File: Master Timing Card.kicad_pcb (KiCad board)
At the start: 4 copper layers, 170 x 100 mm, 250 parts, among them CN1 Pin_03, CN10 M2 x 2.5mm, CN11 UE75-A20-6000T, CN12 U77-A1114-30L1, CN2 Samtec GRF1-J-P-08-E-RA-TH1, CN3 Amphenol 86093488613755E1LF, CN6 SQW-104-01-F-D-VS, CN7 104031-0811, CN8 104031-0811, CN9 TE 1-2199230-6, J1 Connector_RJ45_Magjack_Abraco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, Q1 DMN62D0U-7, Q2 DMN62D0U-7, Q3 DMN62D0U-7, Q4 onsemi FDC6330L, T1 TC2-72T+, T2 TC2-72T+, T3 TC2-72T+, T4 TC2-72T+, T5 TC2-72T+, T6 TC2-72T+, T7 TC2-72T+, T8 TC2-72T+, U1 Microchip 24LC024-E/MC, U2 Analog MAX3483ESA+, U3 TI TPS79301DBV, U4 TI TPS79301DBV, U5 RC32504A000GNK#BB0, U6 RC32504A000GNK#BB0, U7 SN74LVC1G125DBV, U8 SN74LVC1G125DBV

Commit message: Added ESD and tided up PSU
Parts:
- added C123: 22u, Capacitor_SMD:C_1206_3216Metric, F.Cu at (236.7, 46.7)
- added C124: 22u, Capacitor_SMD:C_1206_3216Metric, F.Cu at (236.7, 50.0)
- added D5: TPD4E05U06DQA, Diode_WUT:TPD4E05U06DQA, F.Cu at (63.2, 50.0)
- added D6: TPD4E05U06DQA, Diode_WUT:TPD4E05U06DQA, F.Cu at (61.8, 61.5)
- added LD2: Green, LED_SMD:LED_0603_1608Metric, F.Cu at (235.9, 53.0)
- added R57: 1k0, Resistor_SMD:R_0402_1005Metric, F.Cu at (241.0, 46.0)
- added R58: 100R, Resistor_SMD:R_0402_1005Metric, F.Cu at (241.0, 48.0)
- added R59: 100R, Resistor_SMD:R_0402_1005Metric, F.Cu at (241.0, 50.0)
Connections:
- CN5 pad 102: unconnected-(CN5A-PCIe_CLK_nREQ-Pad102) -> /Pi CM4 - HPIO/~{PCIE_CLK_REQ}
- CN5 pad 109: unconnected-(CN5A-PCIe_nRST-Pad109) -> Net-(CN5A-PCIe_nRST)
- CN9 pad 10: unconnected-(CN9-~{LED1}-Pad10) -> Net-(CN9-~{LED1})
- CN9 pad 12: unconnected-(CN9-3.3V-Pad12) -> 3V3_PCIE
- CN9 pad 14: unconnected-(CN9-3.3V-Pad14) -> 3V3_PCIE
- CN9 pad 16: unconnected-(CN9-3.3V-Pad16) -> 3V3_PCIE
- CN9 pad 18: unconnected-(CN9-3.3V-Pad18) -> 3V3_PCIE
- CN9 pad 2: unconnected-(CN9-3.3V-Pad2) -> 3V3_PCIE
- CN9 pad 4: unconnected-(CN9-3.3V-Pad4) -> 3V3_PCIE
- CN9 pad 41: /Pi CM4 - HPIO/PCIE_PET0_N -> /Pi CM4 - HPIO/PCIE_PER0_N
- CN9 pad 43: /Pi CM4 - HPIO/PCIE_PET0_P -> /Pi CM4 - HPIO/PCIE_PER0_P
- CN9 pad 47: /Pi CM4 - HPIO/PCIE_PER0_N -> /Pi CM4 - HPIO/PCIE_PET0_N
- CN9 pad 49: /Pi CM4 - HPIO/PCIE_PER0_P -> /Pi CM4 - HPIO/PCIE_PET0_P
- CN9 pad 50: unconnected-(CN9-~{PERST}-Pad50) -> /Pi CM4 - HPIO/~{PCIE_RST}
- CN9 pad 52: unconnected-(CN9-~{CLKREQ}-Pad52) -> Net-(CN9-~{CLKREQ})
- CN9 pad 70: unconnected-(CN9-3.3V-Pad70) -> 3V3_PCIE
- CN9 pad 72: unconnected-(CN9-3.3V-Pad72) -> 3V3_PCIE
- CN9 pad 74: unconnected-(CN9-3.3V-Pad74) -> 3V3_PCIE

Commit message: started on power
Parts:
- added C125: 100n, Capacitor_SMD:C_0402_1005Metric, F.Cu at (129.7, 99.3)
- added C126: 22u, Capacitor_SMD:C_1206_3216Metric, F.Cu at (128.2, 90.9)
- added C127: 22u, Capacitor_SMD:C_1206_3216Metric, F.Cu at (128.2, 94.2)
- added C128: 100n, Capacitor_SMD:C_0402_1005Metric, F.Cu at (129.3, 85.1)
- added C129: 10n, Capacitor_SMD:C_0402_1005Metric, F.Cu at (236.8, 62.2)
- added C130: 10u, Capacitor_SMD:C_1206_3216Metric, F.Cu at (232.6, 62.9)
- added C131: 10n, Capacitor_SMD:C_0402_1005Metric, F.Cu at (236.8, 64.1)
- added C132: 10u, Capacitor_SMD:C_1206_3216Metric, F.Cu at (232.6, 66.2)
- added C133: 220p, Capacitor_SMD:C_0402_1005Metric, F.Cu at (236.8, 66.1)
- added C134: 220p, Capacitor_SMD:C_0402_1005Metric, F.Cu at (236.8, 68.1)
- added C135: 100n, Capacitor_SMD:C_0402_1005Metric, F.Cu at (236.8, 70.0)
- added C136: 1u, Capacitor_SMD:C_0402_1005Metric, F.Cu at (236.8, 72.0)
- added C137: 47u, Capacitor_SMD:C_1206_3216Metric, F.Cu at (232.6, 69.5)
- added C138: 47u, Capacitor_SMD:C_1206_3216Metric, F.Cu at (232.6, 72.9)
- added C139: 10p, Capacitor_SMD:C_0402_1005Metric, F.Cu at (236.8, 74.0)
- added C140: 10p, Capacitor_SMD:C_0402_1005Metric, F.Cu at (236.8, 76.0)
- added C141: 47u, Capacitor_SMD:C_1206_3216Metric, F.Cu at (232.6, 76.2)
- added C142: 47u, Capacitor_SMD:C_1206_3216Metric, F.Cu at (232.6, 79.6)
- added CN13: Harwin M20-9990246, Connector_PinHeader_2.54mm:PinHeader_1x02_P2.54mm_Vertical, F.Cu at (123.1, 91.5)
- added CN14: USB4110-GF-A, Connector_WUT:USB-C_GCT_USB4110-GF-A, F.Cu at (40.0, 40.8)
- added D7: 3V3, Diode_SMD:D_SOD-523, F.Cu at (130.1, 97.1)
- added D8: USBLC6-2M6, Diode_WUT:TVS_ST_USBLC6-2M6, F.Cu at (126.4, 85.6)
- added FB25: 1k8, Inductor_SMD:L_0402_1005Metric, F.Cu at (136.8, 75.0)
- added FL1: 90R, Inductor_WUT:L_CommonMode_Wurth_WE-CNSW_0805, F.Cu at (67.8, 38.8)
- added L2: 2u2, Inductor_WUT:Coilcraft_XEL4030, F.Cu at (241.3, 64.2)
- added L3: 2u2, Inductor_WUT:Coilcraft_XEL4030, F.Cu at (241.3, 70.2)
- added LD3: Green, LED_SMD:LED_0603_1608Metric, F.Cu at (122.8, 97.7)
- added R60: 100R, Resistor_SMD:R_0402_1005Metric, F.Cu at (126.8, 98.9)
- added R61: 5k1, Resistor_SMD:R_0402_1005Metric, F.Cu at (136.8, 77.0)
- added R62: 5k1, Resistor_SMD:R_0402_1005Metric, F.Cu at (136.8, 79.0)
- added R63: 0R0, Resistor_SMD:R_0402_1005Metric, F.Cu at (136.8, 81.0)
- added R64: 15k, Resistor_SMD:R_0402_1005Metric, F.Cu at (245.8, 62.2)
- added R65: 120k, Resistor_SMD:R_0402_1005Metric, F.Cu at (245.8, 64.2)
- added R66: 10k, Resistor_SMD:R_0402_1005Metric, F.Cu at (245.8, 66.2)
- added R67: 10k, Resistor_SMD:R_0402_1005Metric, F.Cu at (245.8, 68.1)
- added R68: 0R0, Resistor_SMD:R_0402_1005Metric, F.Cu at (245.8, 70.1)
- added R69: 15k, Resistor_SMD:R_0402_1005Metric, F.Cu at (248.7, 62.2)
- added R70: 0R0, Resistor_SMD:R_0402_1005Metric, F.Cu at (248.7, 64.2)
- added R71: 15k, Resistor_SMD:R_0402_1005Metric, F.Cu at (248.7, 66.2)
- added R73: 300k, Resistor_SMD:R_0402_1005Metric, F.Cu at (248.7, 68.1)
- added R74: 56k, Resistor_SMD:R_0402_1005Metric, F.Cu at (248.7, 70.1)
- added R75: 470k, Resistor_SMD:R_0402_1005Metric, F.Cu at (251.6, 62.2)
- added R76: 150k, Resistor_SMD:R_0402_1005Metric, F.Cu at (251.6, 64.2)
- added R77: 100k, Resistor_SMD:R_0402_1005Metric, F.Cu at (251.6, 66.2)
- added R78: 56m, Resistor_SMD:R_1020_2550Metric, F.Cu at (246.8, 74.5)
- added R79: 56m, Resistor_SMD:R_1020_2550Metric, F.Cu at (251.8, 74.5)
- added U9: Analog LT8650SEV#PBF, IC_WUT:LQFN-32(28)-6EP_6x4mm_P0.5mm_EP1.1x1.33mm, F.Cu at (241.3, 77.5)
- CN7, CN8: footprint Connector_Card:microSD_HC_Molex_104031-0811 -> Connector_WUT:microSD_HC_Molex_104031-0811
- R54: value 0R0 -> 1k0
- moved R54 389.9 mm to (126.8, 96.9), turned to 0 degrees
- moved J1 12.8 mm to (47.5, 59.0)
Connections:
- net /GPS/ANT_VCC renamed /GPS/VCC_ANT
- net /GPS/GNSS_VCC renamed /GPS/VCC_GNSS
- CN4 pad 21: unconnected-(CN4A-PI_nLED_Activity-Pad21) -> Net-(CN4A-PI_nLED_Activity)
- CN4 pad 77: unconnected-(CN4C-+5v_(Input)-Pad77) -> 5V0_PI
- CN4 pad 78: unconnected-(CN4C-GPIO_VREF(1.8v/3.3v_Input)-Pad78) -> /Pi CM4 - GPIO/GPIO_VREF
- CN4 pad 79: unconnected-(CN4C-+5v_(Input)-Pad79) -> 5V0_PI
- CN4 pad 81: unconnected-(CN4C-+5v_(Input)-Pad81) -> 5V0_PI
- CN4 pad 83: unconnected-(CN4C-+5v_(Input)-Pad83) -> 5V0_PI
- CN4 pad 84: unconnected-(CN4C-+3.3v_(Output)-Pad84) -> /Pi CM4 - GPIO/GPIO_VREF
- CN4 pad 85: unconnected-(CN4C-+5v_(Input)-Pad85) -> 5V0_PI
- CN4 pad 86: unconnected-(CN4C-+3.3v_(Output)-Pad86) -> /Pi CM4 - GPIO/GPIO_VREF
- CN4 pad 87: unconnected-(CN4C-+5v_(Input)-Pad87) -> 5V0_PI
- CN5 pad 101: unconnected-(CN5A-USB_OTG_ID-Pad101) -> Net-(CN5A-USB_OTG_ID)
- CN5 pad 103: unconnected-(CN5A-USB2_N-Pad103) -> Net-(CN5A-USB2_N)
- CN5 pad 105: unconnected-(CN5A-USB2_P-Pad105) -> Net-(CN5A-USB2_P)
- D6 pad 1: unconnected-(D6-Pad1) -> Net-(CN4B-Ethernet_Pair2_P)
- D6 pad 10: unconnected-(D6-NC-Pad10) -> Net-(CN4B-Ethernet_Pair2_P)
- D6 pad 2: unconnected-(D6-Pad2) -> Net-(CN4B-Ethernet_Pair2_N)
- D6 pad 3: unconnected-(D6-Pad3) -> 0V
- D6 pad 4: unconnected-(D6-Pad4) -> Net-(CN4B-Ethernet_Pair3_P)
- D6 pad 5: unconnected-(D6-Pad5) -> Net-(CN4B-Ethernet_Pair3_N)
- D6 pad 6: unconnected-(D6-NC-Pad6) -> Net-(CN4B-Ethernet_Pair3_N)
- D6 pad 7: unconnected-(D6-NC-Pad7) -> Net-(CN4B-Ethernet_Pair3_P)
- D6 pad 8: unconnected-(D6-Pad8) -> 0V
- D6 pad 9: unconnected-(D6-NC-Pad9) -> Net-(CN4B-Ethernet_Pair2_N)
- R54 pad 1: 0V -> Net-(LD3-K)
- R54 pad 2: Net-(CN4A-nRPIBOOT) -> Net-(CN4A-PI_nLED_Activity)

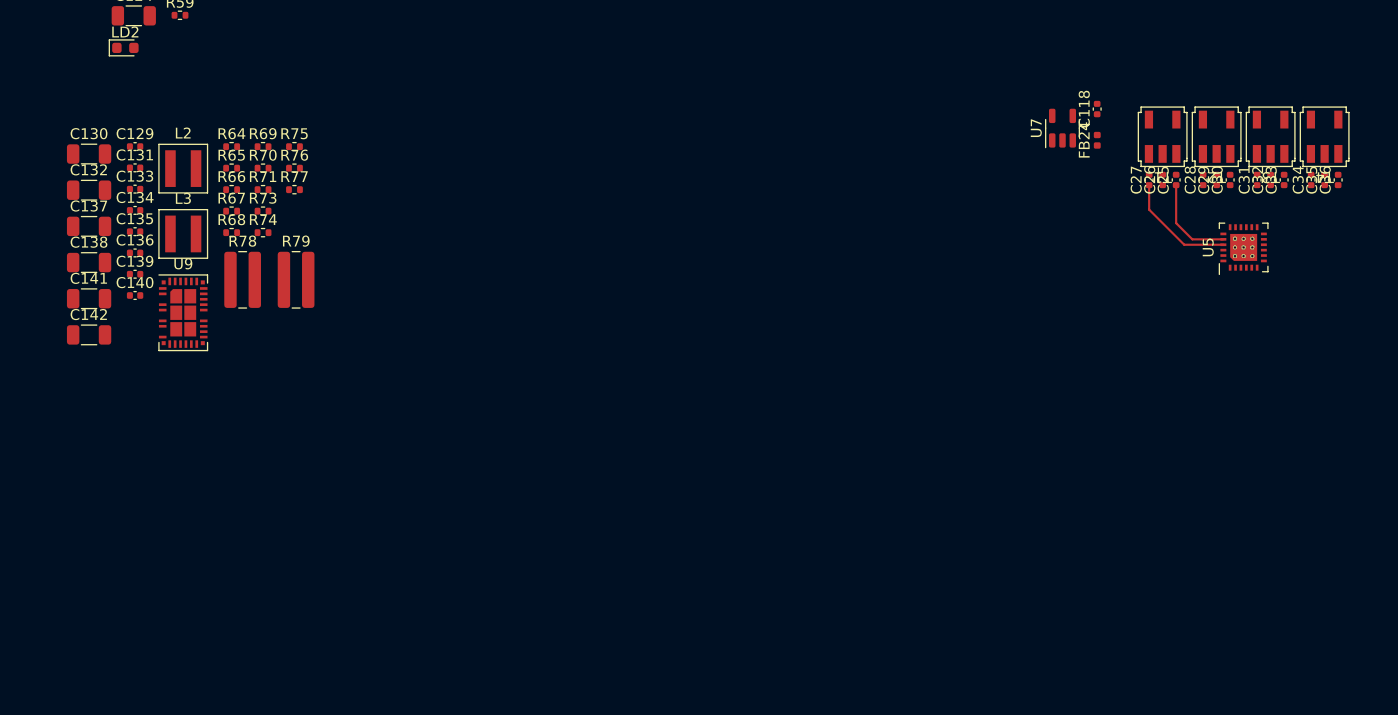
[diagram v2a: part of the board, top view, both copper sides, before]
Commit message: Added power supply
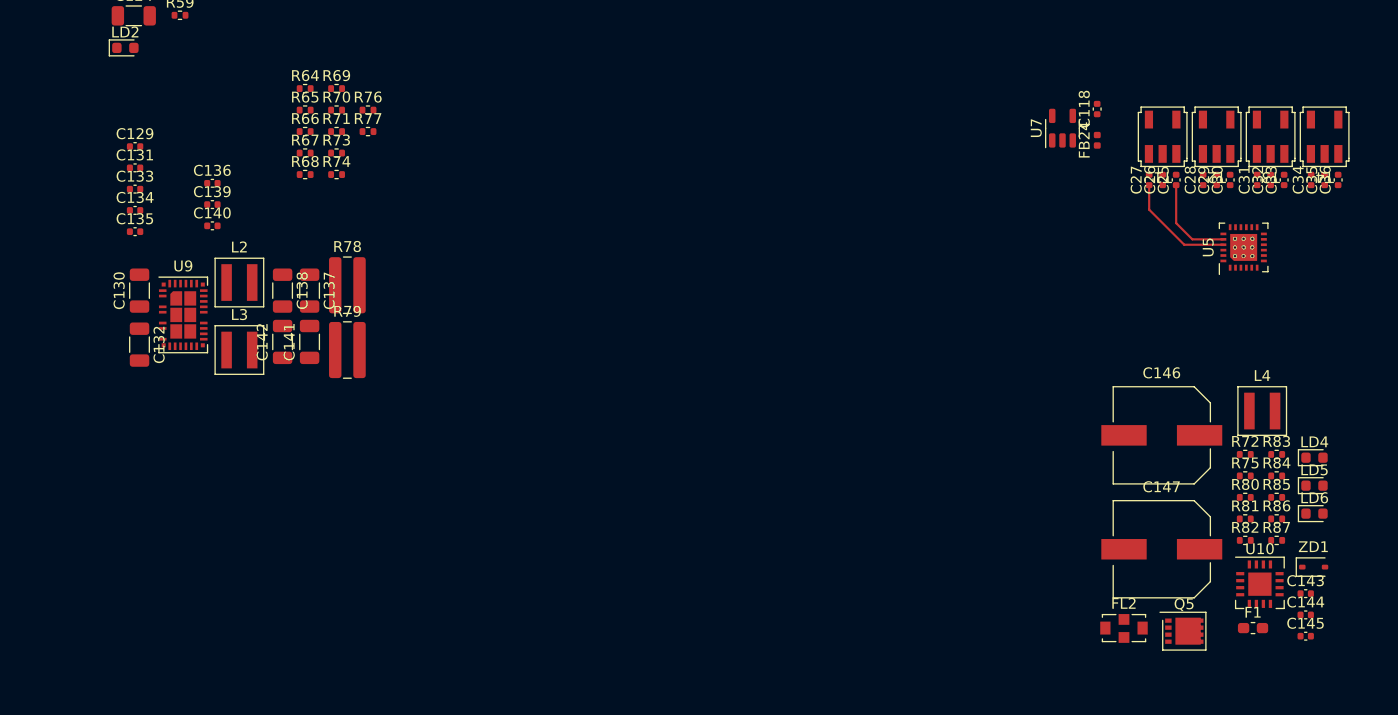
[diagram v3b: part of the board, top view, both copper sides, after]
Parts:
- added C143: 1u, Capacitor_SMD:C_0402_1005Metric, F.Cu at (345.2, 103.6)
- added C144: 1u, Capacitor_SMD:C_0402_1005Metric, F.Cu at (345.2, 105.5)
- added C145: 100n, Capacitor_SMD:C_0402_1005Metric, F.Cu at (345.2, 107.5)
- added C146: 220u, Capacitor_WUT:Wurth_WCAP-HSG5_8x10.5mm_SM, F.Cu at (331.9, 88.9)
- added C147: 220u, Capacitor_WUT:Wurth_WCAP-HSG5_8x10.5mm_SM, F.Cu at (331.9, 99.5)
- added F1: 1A, Fuse:Fuse_0603_1608Metric_Pad1.05x0.95mm_HandSolder, F.Cu at (340.4, 106.8)
- added FL2: NFM31HK153R1H3, Capacitor_WUT:Murata_NFM31HK, F.Cu at (328.4, 106.8)
- added L4: 2u2, Inductor_WUT:Coilcraft_XEL4030, F.Cu at (341.2, 86.7)
- added LD4: Green, LED_SMD:LED_0603_1608Metric, F.Cu at (346.1, 91.0)
- added LD5: Green, LED_SMD:LED_0603_1608Metric, F.Cu at (346.1, 93.6)
- added LD6: Green, LED_SMD:LED_0603_1608Metric, F.Cu at (346.1, 96.2)
- added Q5: TSM085P03CV RGG, IC_WUT:PDFN33-8, F.Cu at (334.0, 107.0)
- added R72: 47k, Resistor_SMD:R_0402_1005Metric, F.Cu at (339.6, 90.7)
- added R80: 6R8, Resistor_SMD:R_0402_1005Metric, F.Cu at (339.6, 94.7)
- added R81: 6R8, Resistor_SMD:R_0402_1005Metric, F.Cu at (339.6, 96.6)
- added R82: 6R8, Resistor_SMD:R_0402_1005Metric, F.Cu at (339.6, 98.6)
- added R83: 4k7, Resistor_SMD:R_0402_1005Metric, F.Cu at (342.6, 90.7)
- added R84: 4k7, Resistor_SMD:R_0402_1005Metric, F.Cu at (342.6, 92.7)
- added R85: 100k, Resistor_SMD:R_0402_1005Metric, F.Cu at (342.6, 94.7)
- added R86: 10k, Resistor_SMD:R_0402_1005Metric, F.Cu at (342.6, 96.6)
- added R87: 47k, Resistor_SMD:R_0402_1005Metric, F.Cu at (342.6, 98.6)
- added U10: INA3221AIRGV, IC_WUT:Texas_VFQN-16-1EP_RGV0016A, F.Cu at (341.0, 102.7)
- added ZD1: 15V, Diode_SMD:D_SOD-323, F.Cu at (346.0, 101.1)
- R75: value 470k -> 6R8
- moved R75 93.2 mm to (339.6, 92.7)
- moved C137 21.3 mm to (253.0, 75.5), turned to -90 degrees
- moved C141 20.8 mm to (253.0, 80.2), turned to 90 degrees
- moved C138 18.1 mm to (250.5, 75.5), turned to -90 degrees
- moved C142 17.9 mm to (250.5, 80.2), turned to 90 degrees
- moved C132 15.0 mm to (237.2, 80.5), turned to -90 degrees
- moved C130 13.5 mm to (237.2, 75.5), turned to 90 degrees
- moved L3 11.9 mm to (246.5, 81.0)
- moved L2 11.8 mm to (246.5, 74.8)
- moved R78 9.71 mm to (256.5, 75.0)
- moved C136 9.64 mm to (244.0, 65.6)
- moved C139 9.64 mm to (244.0, 67.5)
- moved C140 9.64 mm to (244.0, 69.5)
- moved R77 8.68 mm to (258.4, 60.8)
- moved R76 8.68 mm to (258.4, 58.8)
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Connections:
- CN4 pad 78: /Pi CM4 - GPIO/GPIO_VREF -> 3V3
- CN4 pad 84: /Pi CM4 - GPIO/GPIO_VREF -> 3V3
- CN4 pad 86: /Pi CM4 - GPIO/GPIO_VREF -> 3V3
- R75 pad 1: Net-(C140-Pad1) -> /Power Supplies/5V0_SENSE_P
- R75 pad 2: Net-(U9-FB2) -> Net-(C137-Pad1)
- R76 pad 1: Net-(U9-FB2) -> Net-(C140-Pad1)
- R76 pad 2: 0V -> Net-(U9-FB2)
- U9 pad 26: unconnected-(U9-BIAS-Pad26) -> 5V0_PI

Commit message: Schematic mostly done
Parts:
- removed C121: 100n, Capacitor_SMD:C_0402_1005Metric
- removed C144: 1u, Capacitor_SMD:C_0402_1005Metric
- removed CN8: 104031-0811, Connector_WUT:microSD_HC_Molex_104031-0811
- added C148: 10u, Capacitor_SMD:C_0603_1608Metric, F.Cu at (266.8, 100.2)
- added C149: 10u, Capacitor_SMD:C_0603_1608Metric, F.Cu at (266.8, 108.3)
- added C150: 10u, Capacitor_SMD:C_0603_1608Metric, F.Cu at (266.8, 110.8)
- added C151: 1u, Capacitor_SMD:C_0402_1005Metric, F.Cu at (339.5, 141.1)
- added C152: 1u, Capacitor_SMD:C_0402_1005Metric, F.Cu at (339.5, 149.5)
- added C153: 10u, Capacitor_SMD:C_0603_1608Metric, F.Cu at (340.1, 138.8)
- added C154: 100n, Capacitor_SMD:C_0402_1005Metric, F.Cu at (339.5, 143.1)
- added C155: 10u, Capacitor_SMD:C_0603_1608Metric, F.Cu at (340.1, 147.3)
- added C156: 100n, Capacitor_SMD:C_0402_1005Metric, F.Cu at (339.5, 151.5)
- added C157: 100n, Capacitor_SMD:C_0402_1005Metric, F.Cu at (315.1, 142.2)
- added C158: 1u, Capacitor_SMD:C_0402_1005Metric, F.Cu at (331.3, 126.6)
- added CN15: 731385033, Connector_WUT:BNC_Molex_731385033, F.Cu at (239.1, 111.8)
- added D10: 5V0, Diode_SMD:D_SOD-523, F.Cu at (311.3, 120.9)
- added D11: 5V0, Diode_SMD:D_SOD-523, F.Cu at (311.3, 123.3)
- added D12: 5V0, Diode_SMD:D_SOD-523, F.Cu at (311.3, 125.8)
- added D13: 5V0, Diode_SMD:D_SOD-523, F.Cu at (311.3, 128.2)
- added D14: 5V0, Diode_SMD:D_SOD-523, F.Cu at (311.3, 130.7)
- added D15: 5V0, Diode_SMD:D_SOD-523, F.Cu at (311.3, 133.1)
- added D16: 5V0, Diode_SMD:D_SOD-523, F.Cu at (311.3, 135.6)
- added D17: 5V0, Diode_SMD:D_SOD-523, F.Cu at (311.3, 138.0)
- added D18: 3V3, Diode_SMD:D_SOD-523, F.Cu at (328.8, 143.4)
- added D19: 3V3, Diode_SMD:D_SOD-523, F.Cu at (328.8, 145.8)
- added D9: 5V0, Diode_SMD:D_SOD-523, F.Cu at (260.5, 103.8)
- added F2: 250mA, Fuse:Fuse_0603_1608Metric, F.Cu at (269.7, 121.4)
- added FB26: 600R, Inductor_SMD:L_0603_1608Metric, F.Cu at (249.0, 126.2)
- added FB27: 600R, Inductor_SMD:L_0603_1608Metric, F.Cu at (249.0, 128.7)
- added FB28: 600R, Inductor_SMD:L_0603_1608Metric, F.Cu at (266.8, 102.8)
- added FB29: 600R, Inductor_SMD:L_0603_1608Metric, F.Cu at (266.8, 113.3)
- added L5: 1u0, Inductor_SMD:L_0603_1608Metric, F.Cu at (249.0, 131.2)
- added L6: 1u0, Inductor_SMD:L_0603_1608Metric, F.Cu at (249.0, 133.7)
- added LD7: Green, LED_SMD:LED_0603_1608Metric, F.Cu at (269.8, 118.8)
- added LD8: Green, LED_SMD:LED_0603_1608Metric, F.Cu at (311.5, 146.4)
- added LD9: WP130WCP_2EGW, LED_WUT:Kingbright_WP130WCP_2EGW, F.Cu at (317.6, 122.2)
- added Q6: DMN62D0U-7, Package_TO_SOT_SMD:SOT-23, F.Cu at (253.4, 132.5)
- added R100: 33R, Resistor_SMD:R_0402_1005Metric, F.Cu at (251.4, 103.4)
- added R101: 33R, Resistor_SMD:R_0402_1005Metric, F.Cu at (251.4, 105.4)
- added R102: 140R, Resistor_SMD:R_0402_1005Metric, F.Cu at (251.4, 107.4)
- added R103: 180R, Resistor_SMD:R_0402_1005Metric, F.Cu at (251.4, 109.4)
- added R104: 180R, Resistor_SMD:R_0402_1005Metric, F.Cu at (251.4, 111.4)
- added R105: 33R, Resistor_SMD:R_0402_1005Metric, F.Cu at (254.3, 97.5)
- added R106: 33R, Resistor_SMD:R_0402_1005Metric, F.Cu at (254.3, 99.5)
- added R107: 140R, Resistor_SMD:R_0402_1005Metric, F.Cu at (254.3, 101.5)
- added R108: 180R, Resistor_SMD:R_0402_1005Metric, F.Cu at (254.3, 103.4)
- added R109: 180R, Resistor_SMD:R_0402_1005Metric, F.Cu at (254.3, 105.4)
- added R110: 33R, Resistor_SMD:R_0402_1005Metric, F.Cu at (254.3, 107.4)
- added R111: 33R, Resistor_SMD:R_0402_1005Metric, F.Cu at (254.3, 109.4)
- added R112: 140R, Resistor_SMD:R_0402_1005Metric, F.Cu at (254.3, 111.4)
- added R113: 180R, Resistor_SMD:R_0402_1005Metric, F.Cu at (257.2, 97.5)
- added R114: 180R, Resistor_SMD:R_0402_1005Metric, F.Cu at (257.2, 99.5)
- added R115: 22k, Resistor_SMD:R_0402_1005Metric, F.Cu at (257.2, 101.5)
- added R116: 13k, Resistor_SMD:R_0402_1005Metric, F.Cu at (257.2, 103.4)
- added R117: 4k7, Resistor_SMD:R_0402_1005Metric, F.Cu at (266.2, 126.5)
- added R118: 10k, Resistor_SMD:R_0402_1005Metric, F.Cu at (257.2, 105.4)
- added R119: 330R, Resistor_SMD:R_0402_1005Metric, F.Cu at (270.3, 102.0)
- added R120: 330R, Resistor_SMD:R_0402_1005Metric, F.Cu at (270.3, 112.5)
- added R121: 18k, Resistor_SMD:R_0402_1005Metric, F.Cu at (270.3, 104.0)
- added R122: 18k, Resistor_SMD:R_0402_1005Metric, F.Cu at (270.3, 114.5)
- added R123: 22k, Resistor_SMD:R_0402_1005Metric, F.Cu at (336.6, 138.6)
- added R124: 22k, Resistor_SMD:R_0402_1005Metric, F.Cu at (336.6, 147.0)
- added R125: 4k7, Resistor_SMD:R_0402_1005Metric, F.Cu at (336.6, 140.6)
- added R126: 4k7, Resistor_SMD:R_0402_1005Metric, F.Cu at (336.6, 149.0)
- added R127: 100R, Resistor_SMD:R_0402_1005Metric, F.Cu at (336.6, 142.6)
- added R128: 100R, Resistor_SMD:R_0402_1005Metric, F.Cu at (336.6, 151.0)
- added R129: 10k, Resistor_SMD:R_0402_1005Metric, F.Cu at (314.9, 146.1)
- added R130: 6R8, Resistor_SMD:R_0402_1005Metric, F.Cu at (328.4, 132.6)
- added R131: 6R8, Resistor_SMD:R_0402_1005Metric, F.Cu at (328.4, 134.6)
- added R132: 100R, Resistor_SMD:R_0402_1005Metric, F.Cu at (323.5, 128.6)
- added R88: 4k7, Resistor_SMD:R_0402_1005Metric, F.Cu at (266.2, 122.5)
- added R89: 100R, Resistor_SMD:R_0402_1005Metric, F.Cu at (248.4, 97.5)
- added R90: 49R9, Resistor_SMD:R_0402_1005Metric, F.Cu at (248.4, 99.5)
- added R91: 49R9, Resistor_SMD:R_0402_1005Metric, F.Cu at (248.4, 101.5)
- added R92: 49R9, Resistor_SMD:R_0402_1005Metric, F.Cu at (248.4, 103.4)
- added R93: 49R9, Resistor_SMD:R_0402_1005Metric, F.Cu at (248.4, 105.4)
- added R94: 475R, Resistor_SMD:R_0402_1005Metric, F.Cu at (248.4, 107.4)
- added R95: 10R, Resistor_SMD:R_0402_1005Metric, F.Cu at (248.4, 109.4)
- added R96: 10R, Resistor_SMD:R_0402_1005Metric, F.Cu at (248.4, 111.4)
- added R97: 20R, Resistor_SMD:R_0402_1005Metric, F.Cu at (251.4, 97.5)
- added R98: 20R, Resistor_SMD:R_0402_1005Metric, F.Cu at (251.4, 99.5)
- added R99: 51R, Resistor_SMD:R_0402_1005Metric, F.Cu at (251.4, 101.5)
- added T9: TC2-72T+, RF_WUT:MiniCircuits_AT1521, F.Cu at (259.8, 124.0)
- added TP3: ~, TestPoint:TestPoint_Pad_D1.0mm, F.Cu at (260.2, 98.0)
- added TP4: ~, TestPoint:TestPoint_Pad_D1.0mm, F.Cu at (260.2, 101.0)
- added U11: SY75576LKY, Package_SO:TSSOP-20_4.4x6.5mm_P0.65mm, F.Cu at (255.4, 116.4)
- added U12: TI TPS79301DBV, Package_TO_SOT_SMD:SOT-23-6, F.Cu at (259.3, 129.7)
- added U13: LT3045IDD#PBF, Package_DFN_QFN:DFN-10-1EP_3x3mm_P0.5mm_EP1.65x2.38mm_ThermalVias, F.Cu at (271.4, 98.8)
- added U14: LT3045IDD#PBF, Package_DFN_QFN:DFN-10-1EP_3x3mm_P0.5mm_EP1.65x2.38mm_ThermalVias, F.Cu at (271.4, 109.3)
- added U15: SN74LVC1G02DCK, Package_TO_SOT_SMD:SOT-353_SC-70-5, F.Cu at (311.6, 143.2)
- C104, C115, C27, C31, C33, C34: value 100n -> 10u; footprint Capacitor_SMD:C_0402_1005Metric -> Capacitor_SMD:C_0603_1608Metric
- C109, C110, C112: value 100n -> 100p
- C120: value 100n -> 1u
- C30: value 100n -> 15p
- CN1: value Pin_03 -> M20-9990346
- D3: value 5V0 -> TPD4E05U06DQA; footprint Diode_SMD:D_SOD-323 -> Diode_WUT:TPD4E05U06DQA
- D4: value ECLAMP2410P -> TPD4E05U06DQA; footprint Diode_WUT:Semtech_ECLAMP2410P -> Diode_WUT:TPD4E05U06DQA
- R10, R11, R12, R13: value 33R -> 1k0
- R14: value 33R -> 100R
- R15: value 33R -> 150m; footprint Resistor_SMD:R_0402_1005Metric -> Resistor_SMD:R_0603_1608Metric
- R22: value 68k -> 20k
- R23: value 22k -> 6k8
- R35: value 100R -> 4k7
- R73: value 300k -> 160k
- R74: value 56k -> 30k
- R76: value 150k -> 15k
- R8: value 4k7 -> 100R
- moved D3 221.1 mm to (328.5, 139.9), turned to 0 degrees
- moved C120 196.7 mm to (339.1, 123.2), turned to 0 degrees
- moved R23 151.4 mm to (266.2, 120.5)
- moved R22 144.3 mm to (266.2, 118.5)
- moved C104 141.0 mm to (249.0, 123.7)
- moved C112 139.5 mm to (255.3, 127.3)
- moved C113 139.5 mm to (255.3, 129.3)
- moved C106 138.0 mm to (252.4, 129.3)
- moved C107 133.3 mm to (255.3, 121.4)
- moved C109 133.0 mm to (255.3, 123.4)
- moved C110 133.0 mm to (255.3, 125.4)
- moved C115 123.0 mm to (266.8, 97.7)
- moved C36 114.2 mm to (252.4, 127.3), turned to 0 degrees
- moved C34 111.8 mm to (249.0, 121.2), turned to 0 degrees
- moved D4 108.5 mm to (331.6, 139.9), turned to 0 degrees
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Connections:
- C1 pad 1: +3.3V -> 3V3
- C101 pad 1: /PLL and SFP/Frequency Synthesiser 2/SDA -> /PLL and SFP/PLL2_SDA
- C104 pad 1: Net-(U6-OUT0_P) -> Net-(CN11-VccR)
- C104 pad 2: Net-(C104-Pad2) -> 0V
- C106 pad 1: Net-(U6-OUT0_N) -> Net-(CN11-VccR)
- C106 pad 2: Net-(C106-Pad2) -> 0V
- C107 pad 1: Net-(U6-OUT1_P) -> Net-(CN11-VccT)
- C107 pad 2: Net-(C107-Pad2) -> 0V
- C109 pad 1: Net-(U6-OUT1_N) -> /PLL and SFP/~{SFP_PRESENT}
- C109 pad 2: Net-(C109-Pad2) -> 0V
- C110 pad 1: Net-(U6-OUT2_P) -> /PLL and SFP/PLL2_SCL
- C110 pad 2: Net-(C110-Pad2) -> 0V
- C112 pad 1: Net-(U6-OUT2_N) -> /PLL and SFP/PLL2_SDA
- C112 pad 2: Net-(C112-Pad2) -> 0V
- C113 pad 1: Net-(U6-OUT3_P) -> /PLL and SFP/SFP_TX_DISABLE
- C113 pad 2: Net-(C113-Pad2) -> 0V
- C115 pad 1: Net-(U6-OUT3_N) -> /PLL and SFP/Frequency Synthesiser 1/1V8_PLL
- C115 pad 2: Net-(C115-Pad2) -> 0V
- C119 pad 1: /GPS/PTP_PPS -> /CM4 Interfaces/PTP_PPS
- C120 pad 1: 3V3 -> /Pi CM4 - GPIO/3V3_SENSE_N
- C120 pad 2: 0V -> /Pi CM4 - GPIO/3V3_SENSE_P
- C135 pad 1: /Power Supplies/3V3_PCIE_EN -> /Pi CM4 - GPIO/3V3_PCIE_EN
- C139 pad 1: Net-(C137-Pad1) -> 5V0_PI
- C140 pad 1: Net-(C140-Pad1) -> 3V3_PCIE
- C141 pad 1: Net-(C140-Pad1) -> Net-(C141-Pad1)
- C142 pad 1: Net-(C140-Pad1) -> Net-(C141-Pad1)
- C143 pad 1: /Power Supplies/5V0_SENSE_P -> /Power Supplies/PCIE_SENSE_P
- C143 pad 2: /Power Supplies/5V0_SENSE_N -> /Power Supplies/PCIE_SENSE_N
- C18 pad 1: Net-(U4-OUT) -> Net-(C18-Pad1)
- C2 pad 1: +3.3V -> 3V3
- C25 pad 1: Net-(U5-OUT0_P) -> 0V
- C27 pad 1: Net-(U5-OUT0_N) -> Net-(U12-EN)
- C27 pad 2: Net-(C27-Pad2) -> 0V
- C28 pad 1: Net-(U5-OUT1_P) -> Net-(U12-NR)
- C28 pad 2: Net-(C28-Pad2) -> 0V
- C3 pad 1: Net-(CN1-Pin_1) -> Net-(U1-VCC)
- C30 pad 1: Net-(U5-OUT1_N) -> Net-(U11-VDD)
- C30 pad 2: Net-(C30-Pad2) -> Net-(U12-FB)
- C31 pad 1: Net-(U5-OUT2_P) -> Net-(U11-VDD)
- C31 pad 2: Net-(C31-Pad2) -> 0V
- C33 pad 1: Net-(U5-OUT2_N) -> Net-(U11-VDD)
- C33 pad 2: Net-(C33-Pad2) -> 0V
- C34 pad 1: Net-(U5-OUT3_P) -> Net-(C34-Pad1)
- C34 pad 2: Net-(C34-Pad2) -> 0V
- C36 pad 1: Net-(U5-OUT3_N) -> Net-(C34-Pad1)
- C36 pad 2: Net-(C36-Pad2) -> 0V
- C4 pad 1: Net-(C4-Pad1) -> 5V0_PI
- C40 pad 1: 1V8_PLL -> /PLL and SFP/Frequency Synthesiser 1/1V8_PLL
- C41 pad 1: 1V8_PLL -> /PLL and SFP/Frequency Synthesiser 1/1V8_PLL
- C45 pad 1: 1V8_PLL -> /PLL and SFP/Frequency Synthesiser 1/1V8_PLL
- C49 pad 1: 1V8_PLL -> /PLL and SFP/Frequency Synthesiser 1/1V8_PLL
- C53 pad 1: 1V8_PLL -> /PLL and SFP/Frequency Synthesiser 1/1V8_PLL
- C56 pad 1: 1V8_PLL -> /PLL and SFP/Frequency Synthesiser 1/1V8_PLL
- C59 pad 1: 1V8_PLL -> /PLL and SFP/Frequency Synthesiser 1/1V8_PLL
- C60 pad 1: /PLL and SFP/Frequency Synthesiser 1/1v8_VDDA -> /PLL and SFP/Frequency Synthesiser 1/1V8_VDDA
- C61 pad 1: /PLL and SFP/Frequency Synthesiser 1/1v8_VDDA -> /PLL and SFP/Frequency Synthesiser 1/1V8_VDDA
- C67 pad 1: /PLL and SFP/Frequency Synthesiser 1/SCL -> /PLL and SFP/PLL1_SCL
- C68 pad 1: /PLL and SFP/Frequency Synthesiser 1/SDA -> /PLL and SFP/PLL1_SDA
- C69 pad 1: /PLL and SFP/Frequency Synthesiser 1/OE -> /PLL and SFP/OE
- C71 pad 1: 1V8_PLL -> /PLL and SFP/Frequency Synthesiser 2/1V8_PLL
- C72 pad 1: 1V8_PLL -> /PLL and SFP/Frequency Synthesiser 2/1V8_PLL
- C73 pad 1: 1V8_PLL -> /PLL and SFP/Frequency Synthesiser 2/1V8_PLL
- C74 pad 1: 1V8_PLL -> /PLL and SFP/Frequency Synthesiser 2/1V8_PLL
- C75 pad 1: 1V8_PLL -> /PLL and SFP/Frequency Synthesiser 2/1V8_PLL
- C76 pad 1: 1V8_PLL -> /PLL and SFP/Frequency Synthesiser 2/1V8_PLL
- C77 pad 1: 1V8_PLL -> /PLL and SFP/Frequency Synthesiser 2/1V8_PLL
- C84 pad 1: /PLL and SFP/Frequency Synthesiser 2/1v8_VDDA -> /PLL and SFP/Frequency Synthesiser 2/1V8_VDDA
- C91 pad 1: /PLL and SFP/Frequency Synthesiser 2/1v8_VDDA -> /PLL and SFP/Frequency Synthesiser 2/1V8_VDDA
- C97 pad 1: /PLL and SFP/Frequency Synthesiser 2/OE -> /PLL and SFP/OE
- C99 pad 1: /PLL and SFP/Frequency Synthesiser 2/SCL -> /PLL and SFP/PLL2_SCL
- CN11 pad 12: unconnected-(CN11-RD--Pad12) -> Net-(CN11-RD-)
- CN11 pad 13: unconnected-(CN11-RD+-Pad13) -> Net-(CN11-RD+)
- CN11 pad 15: unconnected-(CN11-VccR-Pad15) -> Net-(CN11-VccR)
- CN11 pad 16: unconnected-(CN11-VccT-Pad16) -> Net-(CN11-VccT)
- CN11 pad 18: unconnected-(CN11-TD+-Pad18) -> /PLL and SFP/SFP_TX_P
- CN11 pad 19: unconnected-(CN11-TD--Pad19) -> /PLL and SFP/SFP_TX_N
- CN11 pad 2: unconnected-(CN11-TX_FAULT-Pad2) -> /PLL and SFP/SFP_TX_FAULT_OD
- CN11 pad 3: unconnected-(CN11-TX_DISABLE-Pad3) -> Net-(CN11-TX_DISABLE)
- CN11 pad 4: unconnected-(CN11-MOD_DEF2/SDA-Pad4) -> /PLL and SFP/PLL2_SDA
- CN11 pad 5: unconnected-(CN11-MOD_DEF1/SCL-Pad5) -> /PLL and SFP/PLL2_SCL
- CN11 pad 6: unconnected-(CN11-MOD_DEF0/GND-Pad6) -> /PLL and SFP/~{SFP_PRESENT}
- CN11 pad 7: unconnected-(CN11-RATE_SELECT-Pad7) -> Net-(CN11-RATE_SELECT)
- CN11 pad 8: unconnected-(CN11-LOS-Pad8) -> /PLL and SFP/SFP_LOS_OD
- CN2 pad 1: unconnected-(CN2-In-Pad1) -> /RF1
- CN2 pad 2: unconnected-(CN2-In-Pad2) -> /RF2
- CN2 pad 3: unconnected-(CN2-In-Pad3) -> /RF3
- CN2 pad 4: unconnected-(CN2-In-Pad4) -> /RF4
- CN2 pad 5: unconnected-(CN2-In-Pad5) -> /RF5
- CN2 pad 6: unconnected-(CN2-In-Pad6) -> /RF6
- CN2 pad 7: unconnected-(CN2-In-Pad7) -> /RF7
- CN2 pad 8: unconnected-(CN2-In-Pad8) -> /RF8
- CN3 pad a1: +48V -> Net-(CN3-Pada1)
- CN3 pad a2: +48V -> Net-(CN3-Pada1)
- CN3 pad a4: +24V -> Net-(CN3-Pada4)
- CN3 pad a5: +24V -> Net-(CN3-Pada4)
- CN3 pad a7: +12V -> Net-(CN3-Pada7)
- CN3 pad a8: +12V -> Net-(CN3-Pada7)
- CN3 pad b1: +48V -> unconnected-(CN3-Padb1)
- CN3 pad b2: +48V -> unconnected-(CN3-Padb2)
- CN3 pad b4: +24V -> Net-(CN3-Padb4)
- CN3 pad b5: +24V -> Net-(CN3-Padb4)
- CN3 pad b7: +12V -> Net-(CN3-Padb7)
- CN3 pad b8: +12V -> Net-(CN3-Padb7)
- CN3 pad c1: +48V -> Net-(CN3-Padc1)
- CN3 pad c2: +48V -> Net-(CN3-Padc1)
- CN3 pad c4: +24V -> Net-(CN3-Padc4)
- CN3 pad c5: +24V -> Net-(CN3-Padc4)
- CN3 pad c7: +12V -> Net-(CN3-Padc7)
- CN3 pad c8: +12V -> Net-(CN3-Padc7)
- CN4 pad 24: Net-(CN4D-GPIO26) -> unconnected-(CN4D-GPIO26-Pad24)
- CN4 pad 25: /Pi CM4 - GPIO/SFP_LOS -> /PLL and SFP/SFP_LOS_OD
- CN4 pad 27: Net-(CN4D-GPIO20) -> /PLL and SFP/PLL_LOCK
- CN4 pad 30: /Pi CM4 - GPIO/SFP_SDA -> /PLL and SFP/PLL2_SDA
- CN4 pad 34: /Pi CM4 - GPIO/PLL1_SCL -> /GPS/GNSS_RX
- CN4 pad 37: /Pi CM4 - GPIO/SFP_SCL -> /PLL and SFP/PLL2_SCL
- CN4 pad 39: /Pi CM4 - GPIO/~{SFP_PRESENT} -> /PLL and SFP/~{SFP_PRESENT}
- CN4 pad 40: /Pi CM4 - GPIO/SFP_TX_FAULT -> /PLL and SFP/SFP_TX_FAULT_OD
- CN4 pad 45: Net-(CN4D-GPIO24) -> /Pi CM4 - GPIO/PCIE_PWR_GOOD
- CN4 pad 47: Net-(CN4D-GPIO23) -> /Pi CM4 - GPIO/PWR_CRITICAL
- CN4 pad 48: Net-(CN4D-GPIO27) -> unconnected-(CN4D-GPIO27-Pad48)
- CN4 pad 49: /Pi CM4 - GPIO/GNSS_PPS -> /GPS/GNSS_PPS
- CN4 pad 51: /Pi CM4 - GPIO/UART0_RX -> /RS485_RX
- CN4 pad 54: /Pi CM4 - GPIO/PLL1_SDA -> /GPS/GNSS_TX
- CN4 pad 56: /Pi CM4 - GPIO/PLL0_SCL -> /PLL and SFP/PLL1_SCL
- CN4 pad 58: /Pi CM4 - GPIO/PLL0_SDA -> /PLL and SFP/PLL1_SDA
- CN4 pad 84: 3V3 -> Net-(CN4C-+3.3v_(Output)-Pad84)
- CN4 pad 86: 3V3 -> Net-(CN4C-+3.3v_(Output)-Pad84)
- CN4 pad 88: unconnected-(CN4C-+1.8v_(Output)-Pad88) -> 1V8
- CN4 pad 90: unconnected-(CN4C-+1.8v_(Output)-Pad90) -> 1V8
- D3 pad 1: 3V3 -> /Pi CM4 - HPIO/PCIE_PER0_P
- D3 pad 2: 0V -> /Pi CM4 - HPIO/PCIE_PER0_N
- D4 pad 1: Net-(CN8-DAT1) -> unconnected-(D4-Pad1)
- D4 pad 10: /Pi CM4 - GPIO/SD_DAT3 -> unconnected-(D4-NC-Pad10)
- D4 pad 2: Net-(CN8-DAT0) -> unconnected-(D4-Pad2)
- D4 pad 3: Net-(CN8-CLK) -> 0V
- D4 pad 4: 3V3 -> /Pi CM4 - HPIO/PCIE_REFCLK_P
- D4 pad 5: 3V3 -> /Pi CM4 - HPIO/PCIE_REFCLK_N
- D4 pad 6: Net-(CN8-CMD) -> /Pi CM4 - HPIO/PCIE_REFCLK_N
- D4 pad 7: Net-(CN8-DAT3/CD) -> /Pi CM4 - HPIO/PCIE_REFCLK_P
- D4 pad 8: Net-(CN8-DAT2) -> 0V
- D4 pad 9: /Pi CM4 - GPIO/SD_DAT2 -> unconnected-(D4-NC-Pad9)
- FB1 pad 2: Net-(CN1-Pin_1) -> Net-(U1-VCC)
- FB10 pad 1: 1V8_PLL -> /PLL and SFP/Frequency Synthesiser 1/1V8_PLL
- FB11 pad 1: 1V8_PLL -> /PLL and SFP/Frequency Synthesiser 1/1V8_PLL
- FB12 pad 1: 1V8_PLL -> /PLL and SFP/Frequency Synthesiser 1/1V8_PLL
- FB13 pad 1: 1V8_PLL -> /PLL and SFP/Frequency Synthesiser 1/1V8_PLL
- FB14 pad 1: 1V8_PLL -> /PLL and SFP/Frequency Synthesiser 1/1V8_PLL
- FB14 pad 2: /PLL and SFP/Frequency Synthesiser 1/1v8_VDDA -> /PLL and SFP/Frequency Synthesiser 1/1V8_VDDA
- FB16 pad 1: 1V8_PLL -> /PLL and SFP/Frequency Synthesiser 2/1V8_PLL
- FB17 pad 1: 1V8_PLL -> /PLL and SFP/Frequency Synthesiser 2/1V8_PLL
- FB18 pad 1: 1V8_PLL -> /PLL and SFP/Frequency Synthesiser 2/1V8_PLL
- FB19 pad 1: 1V8_PLL -> /PLL and SFP/Frequency Synthesiser 2/1V8_PLL
- FB20 pad 1: 1V8_PLL -> /PLL and SFP/Frequency Synthesiser 2/1V8_PLL
- FB21 pad 1: 1V8_PLL -> /PLL and SFP/Frequency Synthesiser 2/1V8_PLL
- FB22 pad 1: 1V8_PLL -> /PLL and SFP/Frequency Synthesiser 2/1V8_PLL
- FB22 pad 2: /PLL and SFP/Frequency Synthesiser 2/1v8_VDDA -> /PLL and SFP/Frequency Synthesiser 2/1V8_VDDA
- FB7 pad 1: Net-(U4-OUT) -> Net-(C18-Pad1)
- FB8 pad 1: 1V8_PLL -> /PLL and SFP/Frequency Synthesiser 1/1V8_PLL
- FB9 pad 1: 1V8_PLL -> /PLL and SFP/Frequency Synthesiser 1/1V8_PLL
- L1 pad 1: Net-(C4-Pad1) -> 5V0_PI
- L3 pad 2: Net-(C140-Pad1) -> Net-(C141-Pad1)
- R10 pad 1: Net-(CN4D-GPIO22) -> /Pi CM4 - GPIO/COMMS_RED
- R10 pad 2: /Pi CM4 - GPIO/SD_CLK -> Net-(LD9-Pad4)
- R11 pad 1: Net-(CN4D-GPIO23) -> /Pi CM4 - GPIO/COMMS_GREEN
- R11 pad 2: /Pi CM4 - GPIO/SD_CMD -> Net-(LD9-Pad6)
- R12 pad 1: Net-(CN4D-GPIO24) -> /Pi CM4 - GPIO/STATUS_GREEN
- R12 pad 2: /Pi CM4 - GPIO/SD_DAT0 -> Net-(LD9-Pad3)
- R13 pad 1: Net-(CN4D-GPIO25) -> /Pi CM4 - GPIO/STATUS_RED
- R13 pad 2: /Pi CM4 - GPIO/SD_DAT1 -> Net-(LD9-Pad1)
- R14 pad 1: Net-(CN4D-GPIO26) -> Net-(CN4D-GPIO25)
- R14 pad 2: /Pi CM4 - GPIO/SD_DAT2 -> /GPS/GNSS_RESET
- R15 pad 1: Net-(CN4D-GPIO27) -> Net-(CN4C-+3.3v_(Output)-Pad84)
- R15 pad 2: /Pi CM4 - GPIO/SD_DAT3 -> 3V3
- R19 pad 1: /GPS/PTP_PPS -> /CM4 Interfaces/PTP_PPS
- R2 pad 1: +3V3 -> 3V3
- R2 pad 2: /Pi CM4 - GPIO/PLL0_SDA -> /PLL and SFP/PLL1_SDA
- R3 pad 1: +3V3 -> 3V3
- R3 pad 2: /Pi CM4 - GPIO/PLL0_SCL -> /PLL and SFP/PLL1_SCL
- R31 pad 1: +3V3 -> 3V3
- R31 pad 2: /Pi CM4 - GPIO/SFP_SDA -> /PLL and SFP/PLL2_SDA
- R32 pad 1: +3V3 -> 3V3
- R32 pad 2: /Pi CM4 - GPIO/SFP_SCL -> /PLL and SFP/PLL2_SCL
- R35 pad 1: Net-(CN4D-GPIO20) -> 3V3
- R35 pad 2: /Pi CM4 - GPIO/SFP_RATE_SEL -> /PLL and SFP/SFP_LOS_OD
- R36 pad 2: /Pi CM4 - GPIO/SFP_TX_DISABLE -> /PLL and SFP/SFP_TX_DISABLE
- R37 pad 2: /Pi CM4 - GPIO/RS485_~{RX}/TX -> /RS485_~{R}/W
- R4 pad 1: +3V3 -> 3V3
- R4 pad 2: /Pi CM4 - GPIO/PLL1_SDA -> /PLL and SFP/SFP_TX_FAULT_OD
- R5 pad 2: /Pi CM4 - GPIO/PLL0_OE -> /PLL and SFP/OE
- R67 pad 1: /Power Supplies/3V3_PCIE_EN -> /Pi CM4 - GPIO/3V3_PCIE_EN
- R7 pad 2: /Pi CM4 - GPIO/UART0_TX -> /RS485_TX
- R72 pad 1: Net-(U9-FB2) -> 3V3_PCIE
- R72 pad 2: 0V -> Net-(U9-FB2)
- R73 pad 1: Net-(C137-Pad1) -> 5V0_PI
- R75 pad 1: /Power Supplies/5V0_SENSE_P -> Net-(C141-Pad1)
- R75 pad 2: Net-(C137-Pad1) -> /Power Supplies/PCIE_SENSE_P
- R76 pad 1: Net-(C140-Pad1) -> Net-(U9-FB2)
- R76 pad 2: Net-(U9-FB2) -> 0V
- R77 pad 1: 3V3_PI -> 3V3
- R77 pad 2: /Power Supplies/PCIE_PGOOD -> /Pi CM4 - GPIO/PCIE_PWR_GOOD
- R79 pad 1: Net-(C140-Pad1) -> Net-(C141-Pad1)
- R8 pad 1: +3V3 -> Net-(CN4D-GPIO22)
- R8 pad 2: /Pi CM4 - GPIO/PLL1_SCL -> /Pi CM4 - GPIO/3V3_PCIE_EN
- R80 pad 1: /Power Supplies/5V0_SENSE_N -> 3V3_PCIE
- R80 pad 2: 5V0_PI -> /Power Supplies/PCIE_SENSE_N
- R81 pad 1: /Power Supplies/PCIE_SENSE_P -> 3V3
- R81 pad 2: Net-(C140-Pad1) -> /Pi CM4 - GPIO/3V3_SENSE_N
- R82 pad 1: /Power Supplies/PCIE_SENSE_N -> Net-(CN4C-+3.3v_(Output)-Pad84)
- R82 pad 2: 3V3_PCIE -> /Pi CM4 - GPIO/3V3_SENSE_P
- R85 pad 2: /Power Supplies/POWER_CRITICAL -> /Pi CM4 - GPIO/PWR_CRITICAL
- T1 pad 1: Net-(C25-Pad2) -> Net-(U5-OUT0_P)
- T1 pad 3: Net-(C27-Pad2) -> Net-(U5-OUT0_N)
- T1 pad 6: /PLL and SFP/Frequency Synthesiser 1/RF1 -> /RF1
- T2 pad 1: Net-(C30-Pad2) -> Net-(U5-OUT1_N)
- T2 pad 3: Net-(C28-Pad2) -> Net-(U5-OUT1_P)
- T2 pad 4: /PLL and SFP/Frequency Synthesiser 1/RF2 -> /RF2
- T3 pad 1: Net-(C33-Pad2) -> Net-(U5-OUT2_N)
- T3 pad 3: Net-(C31-Pad2) -> Net-(U5-OUT2_P)
- T3 pad 4: /PLL and SFP/Frequency Synthesiser 1/RF3 -> /RF3
- T4 pad 1: Net-(C36-Pad2) -> Net-(U5-OUT3_N)
- T4 pad 3: Net-(C34-Pad2) -> Net-(U5-OUT3_P)
- T4 pad 4: /PLL and SFP/Frequency Synthesiser 1/RF4 -> /RF4
- T5 pad 1: Net-(C104-Pad2) -> Net-(U6-OUT0_P)
- T5 pad 3: Net-(C106-Pad2) -> Net-(U6-OUT0_N)
- T5 pad 6: /PLL and SFP/Frequency Synthesiser 2/RF1 -> /RF5
- T6 pad 1: Net-(C109-Pad2) -> Net-(U6-OUT1_N)
- T6 pad 3: Net-(C107-Pad2) -> Net-(U6-OUT1_P)
- T6 pad 4: /PLL and SFP/Frequency Synthesiser 2/RF2 -> /RF6
- T7 pad 1: Net-(C112-Pad2) -> Net-(U6-OUT2_N)
- T7 pad 3: Net-(C110-Pad2) -> Net-(U6-OUT2_P)
- T7 pad 4: /PLL and SFP/Frequency Synthesiser 2/RF3 -> /RF7
- T8 pad 1: Net-(C115-Pad2) -> Net-(U6-OUT3_N)
- T8 pad 3: Net-(C113-Pad2) -> Net-(U6-OUT3_P)
- T8 pad 4: /PLL and SFP/Frequency Synthesiser 2/RF4 -> /RF8
- TP2 pad 1: Net-(U4-OUT) -> Net-(C18-Pad1)
- U1 pad 8: Net-(CN1-Pin_1) -> Net-(U1-VCC)
- U10 pad 1: /Power Supplies/POWER_SENSE3_N -> /Pi CM4 - GPIO/3V3_SENSE_N
- U10 pad 2: /Power Supplies/POWER_SENSE3_P -> /Pi CM4 - GPIO/3V3_SENSE_P
- U10 pad 6: /Power Supplies/SCL -> /PLL and SFP/PLL2_SCL
- U10 pad 7: /Power Supplies/SDA -> /PLL and SFP/PLL2_SDA
- U10 pad 9: /Power Supplies/POWER_CRITICAL -> /Pi CM4 - GPIO/PWR_CRITICAL
- U2 pad 1: /RX -> /RS485_RX
- U2 pad 2: /~{R}/W -> /RS485_~{R}/W
- U2 pad 3: /~{R}/W -> /RS485_~{R}/W
- U2 pad 4: /TX -> /RS485_TX
- U2 pad 8: +3.3V -> 3V3
- U5 pad 5: /PLL and SFP/Frequency Synthesiser 1/CLK_P -> /PLL and SFP/PLL1_CLK_P
- U5 pad 6: /PLL and SFP/Frequency Synthesiser 1/CLK_N -> /PLL and SFP/PLL1_CLK_N
- U5 pad 7: /PLL and SFP/Frequency Synthesiser 1/OE -> /PLL and SFP/OE
- U5 pad 8: /PLL and SFP/Frequency Synthesiser 1/SCL -> /PLL and SFP/PLL1_SCL
- U5 pad 9: /PLL and SFP/Frequency Synthesiser 1/SDA -> /PLL and SFP/PLL1_SDA
- U6 pad 5: /PLL and SFP/Frequency Synthesiser 2/CLK_P -> /PLL and SFP/PLL2_CLK_P
- U6 pad 6: /PLL and SFP/Frequency Synthesiser 2/CLK_N -> /PLL and SFP/PLL2_CLK_N
- U6 pad 7: /PLL and SFP/Frequency Synthesiser 2/OE -> /PLL and SFP/OE
- U6 pad 8: /PLL and SFP/Frequency Synthesiser 2/SCL -> /PLL and SFP/PLL2_SCL
- U6 pad 9: /PLL and SFP/Frequency Synthesiser 2/SDA -> /PLL and SFP/PLL2_SDA
- U9 pad 12: /Power Supplies/3V3_PCIE_EN -> /Pi CM4 - GPIO/3V3_PCIE_EN
- U9 pad 15: /Power Supplies/PCIE_PGOOD -> /Pi CM4 - GPIO/PCIE_PWR_GOOD
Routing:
- net 3V3: track 0.00 -> 5.09 mm, vias 0 -> 1
- net +3.3V: track 5.09 -> 0.00 mm, vias 1 -> 0
- net /~{R}/W: track 4.06 -> 0.00 mm, vias 1 -> 0
- net /RS485_~{R}/W: track 0.00 -> 4.06 mm, vias 0 -> 1
- net /TX: track 1.79 -> 0.00 mm, vias 1 -> 0
- net /RX: track 1.79 -> 0.00 mm, vias 1 -> 0
- net /RS485_TX: track 0.00 -> 1.79 mm, vias 0 -> 1
- net /RS485_RX: track 0.00 -> 1.79 mm, vias 0 -> 1
